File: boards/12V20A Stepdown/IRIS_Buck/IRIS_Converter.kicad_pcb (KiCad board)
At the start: 4 copper layers, 52.5 x 42 mm, 31 parts, among them J1 TB005-762-02BE, J2 TB005-762-02BE, Q1 CSD17571Q2, Q2 CSD16340Q3, U1 LM25145RGYR

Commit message: iris silkscreen stuff for 20a board
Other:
- board text added: "Electrical leads:"
- board text added: "Hriday, Janine"
- board text added: "Members:"
- board text added: "Nathan, Ozan, Irmak, Aadarsh, Abhinav, Josh"

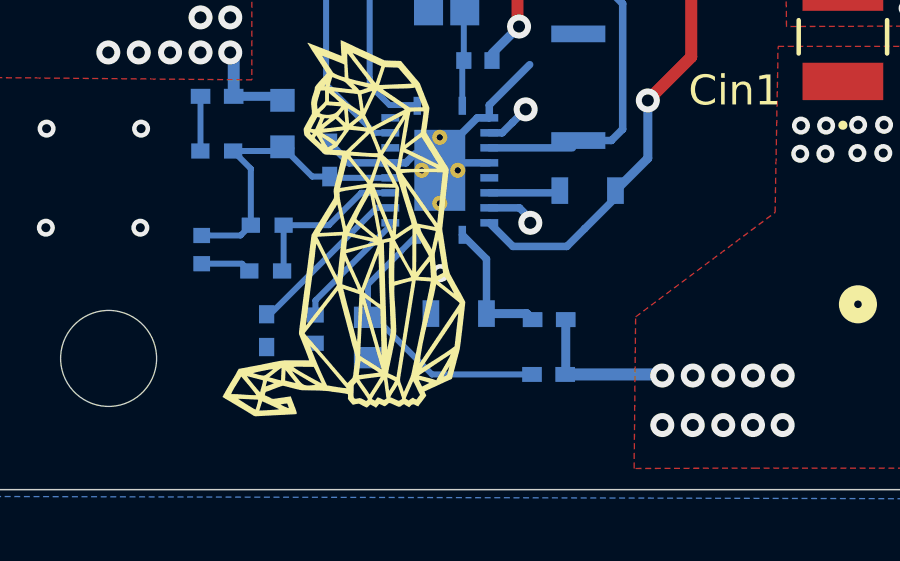
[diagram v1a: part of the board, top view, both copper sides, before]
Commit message: moved en/vulo trace to higher gnd layer
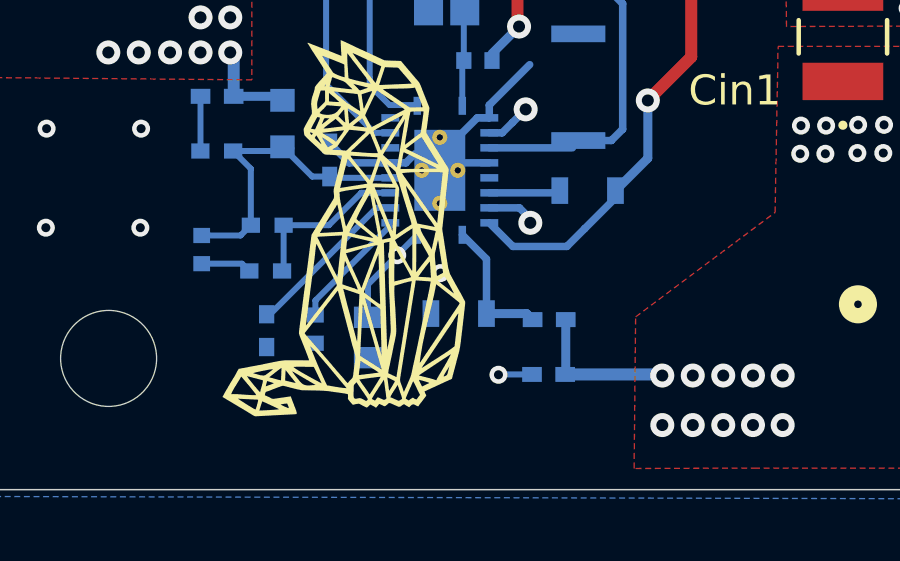
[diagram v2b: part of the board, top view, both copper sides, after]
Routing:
- net /EN/UVLO: track 9.69 -> 11.1 mm, vias 0 -> 2
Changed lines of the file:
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@@
 		(net 11)
+	)
+	(via
+		(at 92.7862 76.2762)
+		(size 0.6)
+		(drill 0.3)
+		(layers "F.Cu" "B.Cu")
+		(net 12)
+	)
+	(via
+		(at 89.4111 72.2915)
+		(size 0.6)
+		(drill 0.3)
+		(layers "F.Cu" "B.Cu")
+		(net 12)
 	)
 	(segment
 		(start 88.437151 74.360751)
 		(end 88.665751 74.360751)
+		(width 0.2)
+		(layer "B.Cu")
+		(net 12)
+	)
+	(segment
+		(start 93.904152 76.265751)
+		(end 92.796649 76.265751)
 		(width 0.2)
 		(layer "B.Cu")
@@
 	)
 	(segment
-		(start 90.570751 76.265751)
-		(end 93.904152 76.265751)
+		(start 92.796649 76.265751)
+		(end 92.7862 76.2762)
+		(width 0.2)
+		(layer "B.Cu")
+		(net 12)
+	)
+	(segment
+		(start 89.4111 72.2915)
+		(end 88.437151 73.265449)
 		(width 0.2)
 		(layer "B.Cu")
@@
 	)
 	(segment
-		(start 88.665751 74.360751)
-		(end 90.570751 76.265751)
+		(start 89.548401 72.154199)
+		(end 89.4111 72.2915)
 		(width 0.2)
 		(layer "B.Cu")
@@
 	)
 	(segment
-		(start 89.548401 72.154199)
-		(end 88.437151 73.265449)
+		(start 89.4111 74.5775)
+		(end 89.4111 72.2915)
 		(width 0.2)
-		(layer "B.Cu")
+		(layer "In2.Cu")
 		(net 12)
 	)
+	(segment
+		(start 92.7862 76.2762)
+		(end 91.1098 76.2762)
+		(width 0.2)
+		(layer "In2.Cu")
+		(net 12)
+	)
+	(segment
+		(start 91.1098 76.2762)
+		(end 89.4111 74.5775)
+		(width 0.2)
+		(layer "In2.Cu")
+		(net 12)
+	)

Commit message: minor fixes
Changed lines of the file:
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@@
 	)
 	(segment
-		(start 96.3676 61.4172)
-		(end 96.3676 61.7982)
+		(start 88.653402 68.2112)
+		(end 87.63 67.187798)
 		(width 0.2)
 		(layer "B.Cu")
@@
 	)
 	(segment
-		(start 87.040151 66.4972)
-		(end 87.040151 63.683449)
+		(start 87.63 67.187798)
+		(end 87.63 63.0936)
 		(width 0.2)
 		(layer "B.Cu")
@@
 	)
 	(segment
-		(start 87.040151 63.683449)
-		(end 90.1192 60.6044)
-		(width 0.2)
-		(layer "B.Cu")
-		(net 22)
-	)
-	(segment
-		(start 87.040151 66.597949)
-		(end 87.040151 66.4972)
-		(width 0.2)
-		(layer "B.Cu")
-		(net 22)
-	)
-	(segment
-		(start 88.653402 68.2112)
-		(end 87.040151 66.597949)
+		(start 96.3676 61.4172)
+		(end 96.3676 61.7982)
 		(width 0.2)
 		(layer "B.Cu")
@@
 		(width 0.2)
 		(layer "B.Cu")
+		(net 22)
+	)
+	(segment
+		(start 87.63 63.0936)
+		(end 90.1192 60.6044)
+		(width 0.2)
+		(layer "B.Cu")

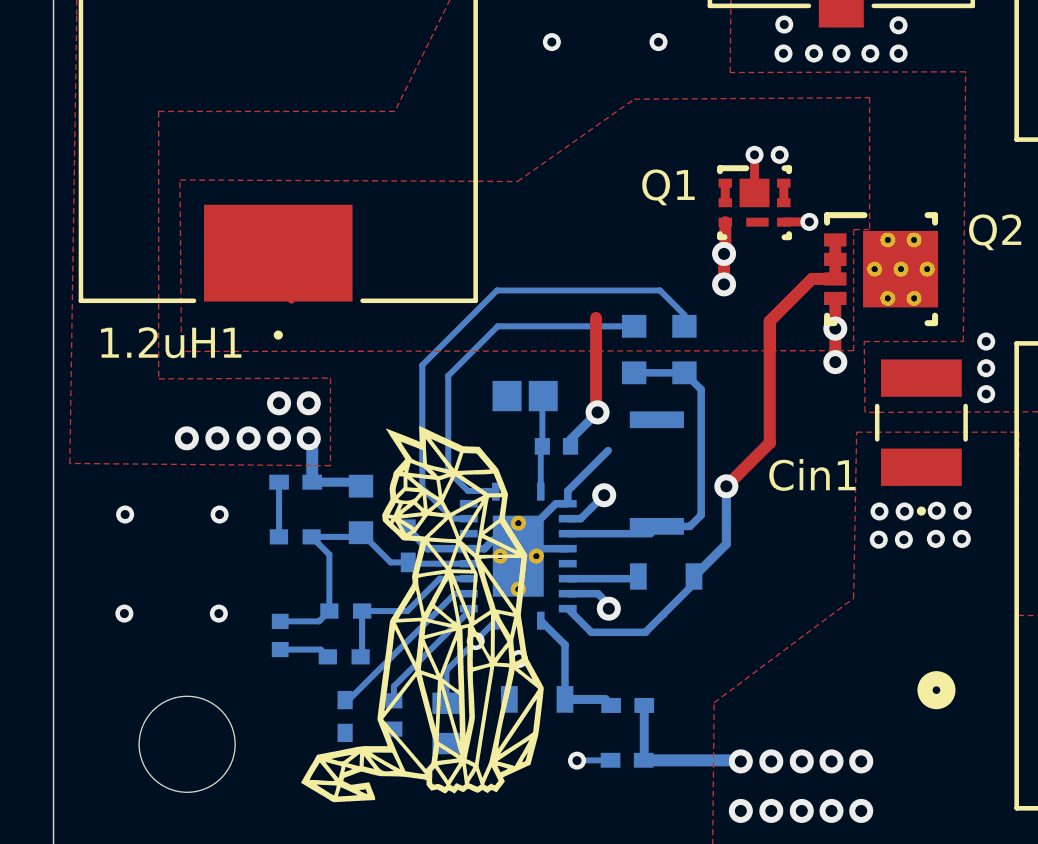
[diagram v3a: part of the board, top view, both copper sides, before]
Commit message: Made gnd planes more continuous
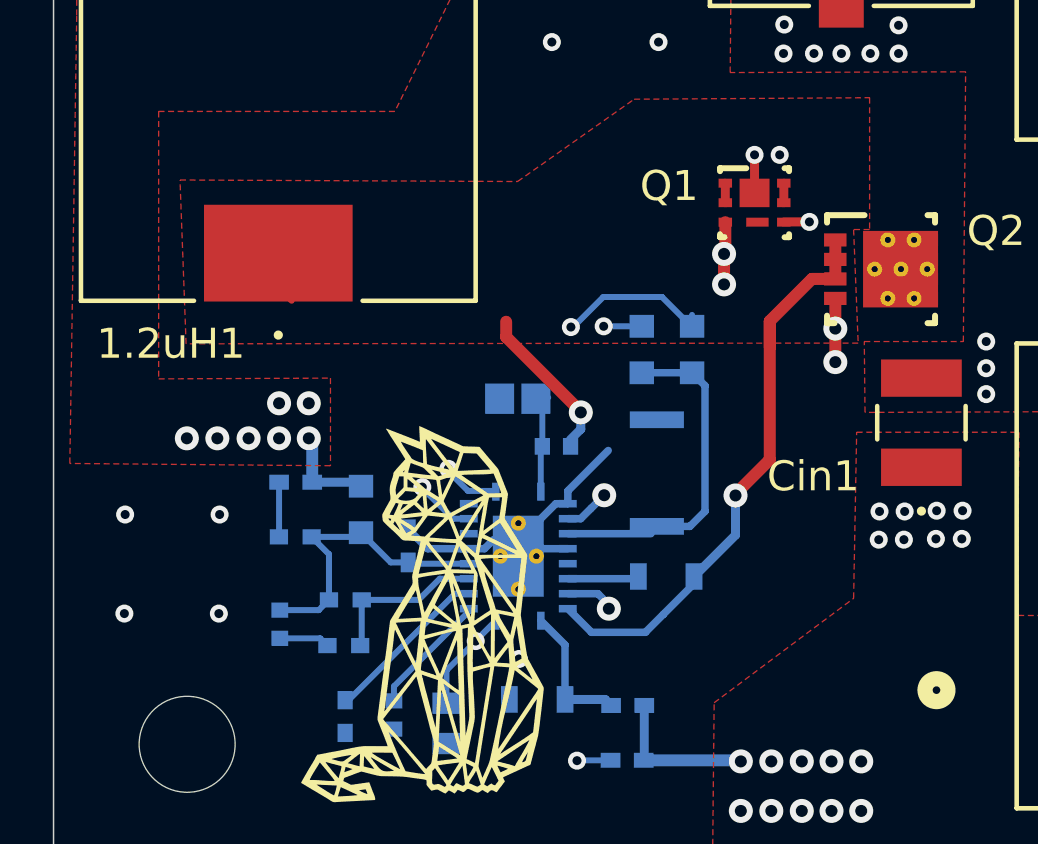
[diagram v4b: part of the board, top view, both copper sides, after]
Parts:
- moved Ccomp1 0.37 mm to (85.0, 72.4)
- moved Ccomp2 0.37 mm to (85.1, 70.9)
- moved Rcomp1 0.37 mm to (82.9, 71.7)
- moved Cilim1 0.26 mm to (90.8, 64.2)
- moved Rpgood1 0.25 mm to (94.9, 62.6)
- moved Rvcc1 0.25 mm to (96.6, 62.6)
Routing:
- net /SW: track 28.1 -> 28.8 mm
- net Net-(U1-PGOOD): track 11.9 -> 12.1 mm, vias 0 -> 2
- net /SYNCin: vias 0 -> 2

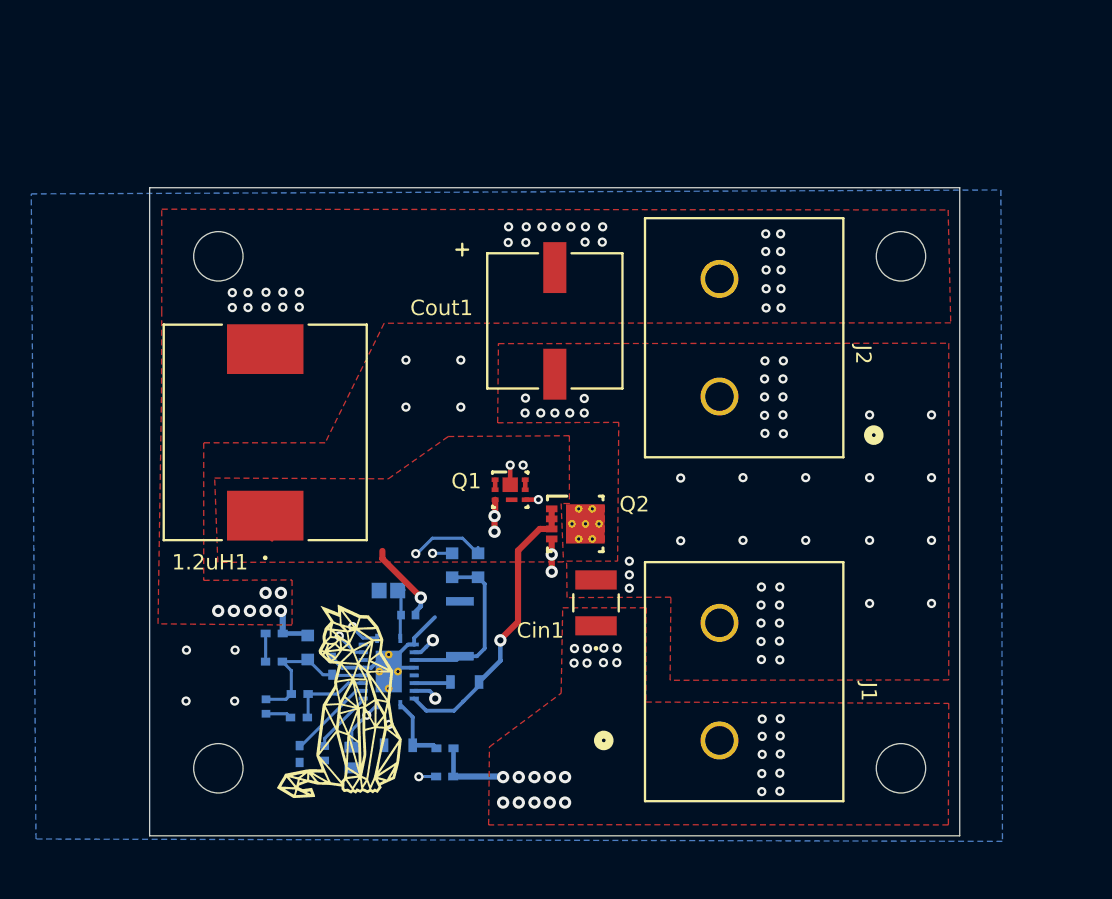
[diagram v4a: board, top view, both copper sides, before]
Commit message: 10a stepdown and 20a stepdown update
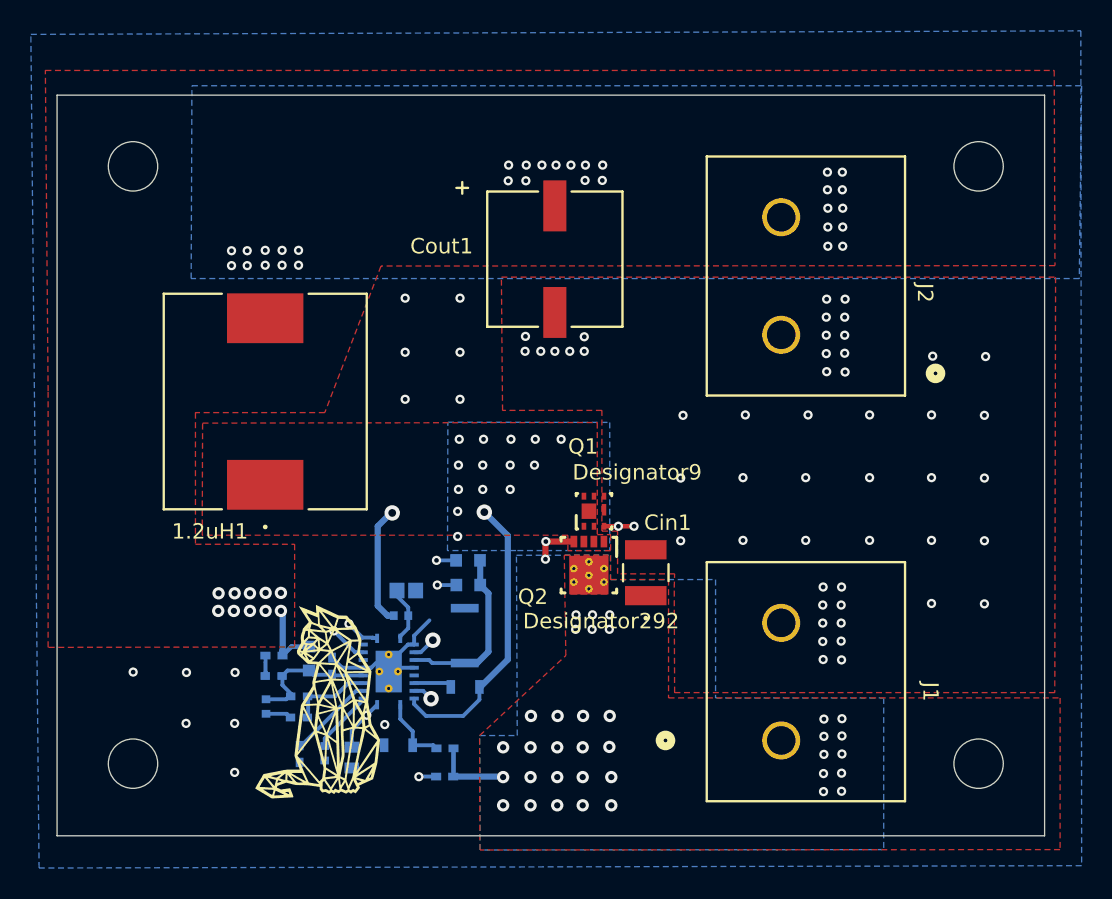
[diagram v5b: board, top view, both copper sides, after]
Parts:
- moved REF** 8.04 mm to (74.3, 36.7)
- moved REF** 7.70 mm to (129.1, 36.7)
- moved J2 5.66 mm to (116.3, 47.6)
- moved Q1 5.61 mm to (104.1, 59.1), turned to 90 degrees
- moved REF** 5.54 mm to (74.3, 75.4)
- moved REF** 5.04 mm to (129.1, 75.4)
- moved Cout1 4.00 mm to (101.6, 42.7)
- moved J1 4.00 mm to (116.3, 73.9)
- moved Cin1 3.77 mm to (107.5, 63.1)
- moved Q2 2.81 mm to (103.8, 62.6), turned to -90 degrees
- moved 1.2uH1 2.00 mm to (82.8, 52.0)
- moved Rpgood1 1.65 mm to (96.0, 63.9), turned to 0 degrees
- moved Rcomp2 1.43 mm to (83.4, 68.4)
- moved Cilim1 1.16 mm to (92.0, 64.2), turned to 0 degrees
- moved Ccomp3 0.93 mm to (83.4, 69.7)
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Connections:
- Q1 pad 7: /SW -> GND
- Q1 pad 8: GND -> /SW
- Q2 pad 5: GND -> /Vin
- Q2 pad 6: GND -> /Vin
- Q2 pad 7: GND -> /Vin
- Q2 pad 8: GND -> /Vin
- Q2 pad 9: GND -> /Vin
- Q2 pad V: GND -> /Vin
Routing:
- net Net-(U1-LO): track 12.9 -> 26.9 mm
- net /SYNCin: track 16.6 -> 13.6 mm
- net Net-(U1-HO): track 17.2 -> 19.8 mm
- net GND: track 13.4 -> 10.9 mm, vias 56 -> 62
- net /Vout: track 3.32 -> 5.28 mm, vias 38 -> 41
- net /SW: track 28.8 -> 27.0 mm, vias 2 -> 16
- net Net-(U1-FB): track 9.99 -> 8.73 mm
- net Net-(U1-VCC): track 12.1 -> 11.4 mm
- net Net-(U1-ILIM): track 3.24 -> 3.76 mm
- net /Vin: vias 28 -> 35
- added copper zone on B.Cu, net /SW
- added copper zone on B.Cu, net /Vin
- added copper zone on B.Cu, net /Vout
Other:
- board size 52.5 x 42 mm -> 64 x 48 mm
- board text added: "20A current paths: High-side MOSFET source/ Low-side MOSFET drain -> IND SW IND Vout -> CAP Vout Cap Vout -> Vout terminal GND Plane 10A current paths Vin terminal -> CAP Vin"
- board text added: "20A/10A 0.070mm = 2 oz/ft^3 20°C Temp Rise"

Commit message: moved 20a terminal vias and some 10a stuff
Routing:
- net GND: vias 62 -> 61
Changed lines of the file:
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@@
 	)
 	(via
-		(at 118.9858 63.9826)
+		(at 125.4 63.9)
 		(size 0.6)
 		(drill 0.3)
@@
 	)
 	(via
-		(at 120.3828 47.6636)
+		(at 110.5246 47.7868)
 		(size 0.6)
 		(drill 0.3)
@@
 	)
 	(via
-		(at 118.9858 68.6816)
-		(size 0.6)
-		(drill 0.3)
-		(layers "F.Cu" "B.Cu")
-		(free yes)
-		(net 6)
-	)
-	(via
-		(at 120.4082 45.3268)
-		(size 0.6)
-		(drill 0.3)
-		(layers "F.Cu" "B.Cu")
-		(free yes)
-		(net 6)
-	)
-	(via
-		(at 120.1542 65.151)
-		(size 0.6)
-		(drill 0.3)
-		(layers "F.Cu" "B.Cu")
-		(free yes)
-		(net 6)
-	)
-	(via
-		(at 119.189 46.4952)
-		(size 0.6)
-		(drill 0.3)
-		(layers "F.Cu" "B.Cu")
-		(free yes)
-		(net 6)
-	)
-	(via
-		(at 120.1796 68.707)
+		(at 125.4 68.599)
+		(size 0.6)
+		(drill 0.3)
+		(layers "F.Cu" "B.Cu")
+		(free yes)
+		(net 6)
+	)
+	(via
+		(at 110.55 45.45)
+		(size 0.6)
+		(drill 0.3)
+		(layers "F.Cu" "B.Cu")
+		(free yes)
+		(net 6)
+	)
+	(via
+		(at 126.5684 65.0684)
+		(size 0.6)
+		(drill 0.3)
+		(layers "F.Cu" "B.Cu")
+		(free yes)
+		(net 6)
+	)
+	(via
+		(at 109.3308 46.6184)
+		(size 0.6)
+		(drill 0.3)
+		(layers "F.Cu" "B.Cu")
+		(free yes)
+		(net 6)
+	)
+	(via
+		(at 126.5938 68.6244)
 		(size 0.6)
 		(drill 0.3)
@@
 	)
 	(via
-		(at 120.1542 67.4878)
-		(size 0.6)
-		(drill 0.3)
-		(layers "F.Cu" "B.Cu")
-		(free yes)
-		(net 6)
-	)
-	(via
-		(at 119.2144 50.0258)
+		(at 126.5684 67.4052)
+		(size 0.6)
+		(drill 0.3)
+		(layers "F.Cu" "B.Cu")
+		(free yes)
+		(net 6)
+	)
+	(via
+		(at 109.3562 50.149)
 		(size 0.6)
 		(drill 0.3)
@@
 	)
 	(via
-		(at 120.4082 50.0512)
+		(at 110.55 50.1744)
 		(size 0.6)
 		(drill 0.3)
@@
 	)
 	(via
-		(at 118.9604 66.3194)
+		(at 125.3746 66.2368)
 		(size 0.6)
 		(drill 0.3)
@@
 	)
 	(via
-		(at 118.9604 65.151)
+		(at 125.3746 65.0684)
 		(size 0.6)
 		(drill 0.3)
@@
 	)
 	(via
-		(at 119.2144 45.3268)
-		(size 0.6)
-		(drill 0.3)
-		(layers "F.Cu" "B.Cu")
-		(free yes)
-		(net 6)
-	)
-	(via
-		(at 119.189 47.6636)
-		(size 0.6)
-		(drill 0.3)
-		(layers "F.Cu" "B.Cu")
-		(free yes)
-		(net 6)
-	)
-	(via
-		(at 126.0094 65.0494)
-		(size 0.6)
-		(drill 0.3)
-		(layers "F.Cu" "B.Cu")
-		(free yes)
-		(net 6)
-	)
-	(via
-		(at 120.1796 63.9826)
-		(size 0.6)
-		(drill 0.3)
-		(layers "F.Cu" "B.Cu")
-		(free yes)
-		(net 6)
-	)
-	(via
-		(at 120.3828 48.832)
+		(at 109.3562 45.45)
+		(size 0.6)
+		(drill 0.3)
+		(layers "F.Cu" "B.Cu")
+		(free yes)
+		(net 6)
+	)
+	(via
+		(at 109.3308 47.7868)
+		(size 0.6)
+		(drill 0.3)
+		(layers "F.Cu" "B.Cu")
+		(free yes)
+		(net 6)
+	)
+	(via
+		(at 126.5938 63.9)
+		(size 0.6)
+		(drill 0.3)
+		(layers "F.Cu" "B.Cu")
+		(free yes)
+		(net 6)
+	)
+	(via
+		(at 110.5246 48.9552)
 		(size 0.6)
 		(drill 0.3)
@@
 	)
 	(via
-		(at 120.1542 66.3194)
+		(at 126.5684 66.2368)
 		(size 0.6)
 		(drill 0.3)
@@
 	)
 	(via
-		(at 118.9604 67.5132)
+		(at 125.3746 67.4306)
 		(size 0.6)
 		(drill 0.3)
@@
 	)
 	(via
-		(at 120.3828 46.4952)
+		(at 110.5246 46.6184)
 		(size 0.6)
 		(drill 0.3)
@@
 	)
 	(via
-		(at 119.189 48.8574)
+		(at 109.3308 48.9806)
 		(size 0.6)
 		(drill 0.3)
@@
 	)
 	(via
-		(at 119.2652 37.0972)
+		(at 109.407 37.2204)
 		(size 0.6)
 		(drill 0.3)
@@
 	)
 	(via
-		(at 119.2906 41.8978)
+		(at 109.4324 42.021)
 		(size 0.6)
 		(drill 0.3)
@@
 	)
 	(via
-		(at 119.2906 40.6532)
-		(size 0.6)
-		(drill 0.3)
-		(layers "F.Cu" "B.Cu")
-		(free yes)
-		(net 19)
-	)
-	(via
-		(at 120.2558 39.434)
+		(at 109.4324 40.7764)
+		(size 0.6)
+		(drill 0.3)
+		(layers "F.Cu" "B.Cu")
+		(free yes)
+		(net 19)
+	)
+	(via
+		(at 110.3976 39.5572)
 		(size 0.6)
 		(drill 0.3)
@@
 	)
 	(via
-		(at 119.2652 38.2402)
+		(at 109.407 38.3634)
 		(size 0.6)
 		(drill 0.3)
@@
 	)
 	(via
-		(at 120.2304 38.2402)
+		(at 110.3722 38.3634)
 		(size 0.6)
 		(drill 0.3)
@@
 	)
 	(via
-		(at 120.2558 41.8978)
-		(size 0.6)
-		(drill 0.3)
-		(layers "F.Cu" "B.Cu")
-		(free yes)
-		(net 19)
-	)
-	(via
-		(at 120.2304 37.0972)
+		(at 110.3976 42.021)
+		(size 0.6)
+		(drill 0.3)
+		(layers "F.Cu" "B.Cu")
+		(free yes)
+		(net 19)
+	)
+	(via
+		(at 110.3722 37.2204)
 		(size 0.6)
 		(drill 0.3)
@@
 	)
 	(via
-		(at 120.2558 40.6532)
-		(size 0.6)
-		(drill 0.3)
-		(layers "F.Cu" "B.Cu")
-		(free yes)
-		(net 19)
-	)
-	(via
-		(at 119.2906 39.434)
+		(at 110.3976 40.7764)
+		(size 0.6)
+		(drill 0.3)
+		(layers "F.Cu" "B.Cu")
+		(free yes)
+		(net 19)
+	)
+	(via
+		(at 109.4324 39.5572)
 		(size 0.6)
 		(drill 0.3)
@@
 	)
 	(via
-		(at 119.0366 72.5424)
+		(at 109.4 72.5424)
 		(size 0.6)
 		(drill 0.3)
@@
 	)
 	(via
-		(at 119.0366 73.66)
+		(at 109.4 73.66)
 		(size 0.6)
 		(drill 0.3)
@@
 	)
 	(via
-		(at 120.205 74.803)
+		(at 110.5684 74.803)
 		(size 0.6)
 		(drill 0.3)
@@
 	)
 	(via
-		(at 120.1796 77.216)
+		(at 110.543 77.216)
 		(size 0.6)
 		(drill 0.3)
@@
 	)
 	(via
-		(at 120.205 72.517)
+		(at 110.5684 72.517)
 		(size 0.6)
 		(drill 0.3)
@@
 	)
 	(via
-		(at 119.0366 74.8284)
-		(size 0.6)
-		(drill 0.3)
-		(layers "F.Cu" "B.Cu")
-		(free yes)
-		(net 20)
-	)
-	(via
-		(at 120.205 73.6346)
+		(at 109.4 74.8284)
+		(size 0.6)
+		(drill 0.3)
+		(layers "F.Cu" "B.Cu")
+		(free yes)
+		(net 20)
+	)
+	(via
+		(at 110.5684 73.6346)
 		(size 0.6)
 		(drill 0.3)
@@
 	)
 	(via
-		(at 120.1796 76.0476)
-		(size 0.6)
-		(drill 0.3)
-		(layers "F.Cu" "B.Cu")
-		(free yes)
-		(net 20)
-	)
-	(via
-		(at 119.0112 77.2414)
+		(at 110.543 76.0476)
+		(size 0.6)
+		(drill 0.3)
+		(layers "F.Cu" "B.Cu")
+		(free yes)
+		(net 20)
+	)
+	(via
+		(at 109.3746 77.2414)
 		(size 0.6)
 		(drill 0.3)
@@
 	)
 	(via
-		(at 119.0112 76.073)
-		(size 0.6)
-		(drill 0.3)
+		(at 109.3746 76.073)
+		(size 0.6)
+		(drill 0.3)
